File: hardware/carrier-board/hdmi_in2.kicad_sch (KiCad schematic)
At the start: 3 parts, among them J1 HDMI_TypeA_Receptacle, Q1 2N7002, U1 TXS0102DCUR

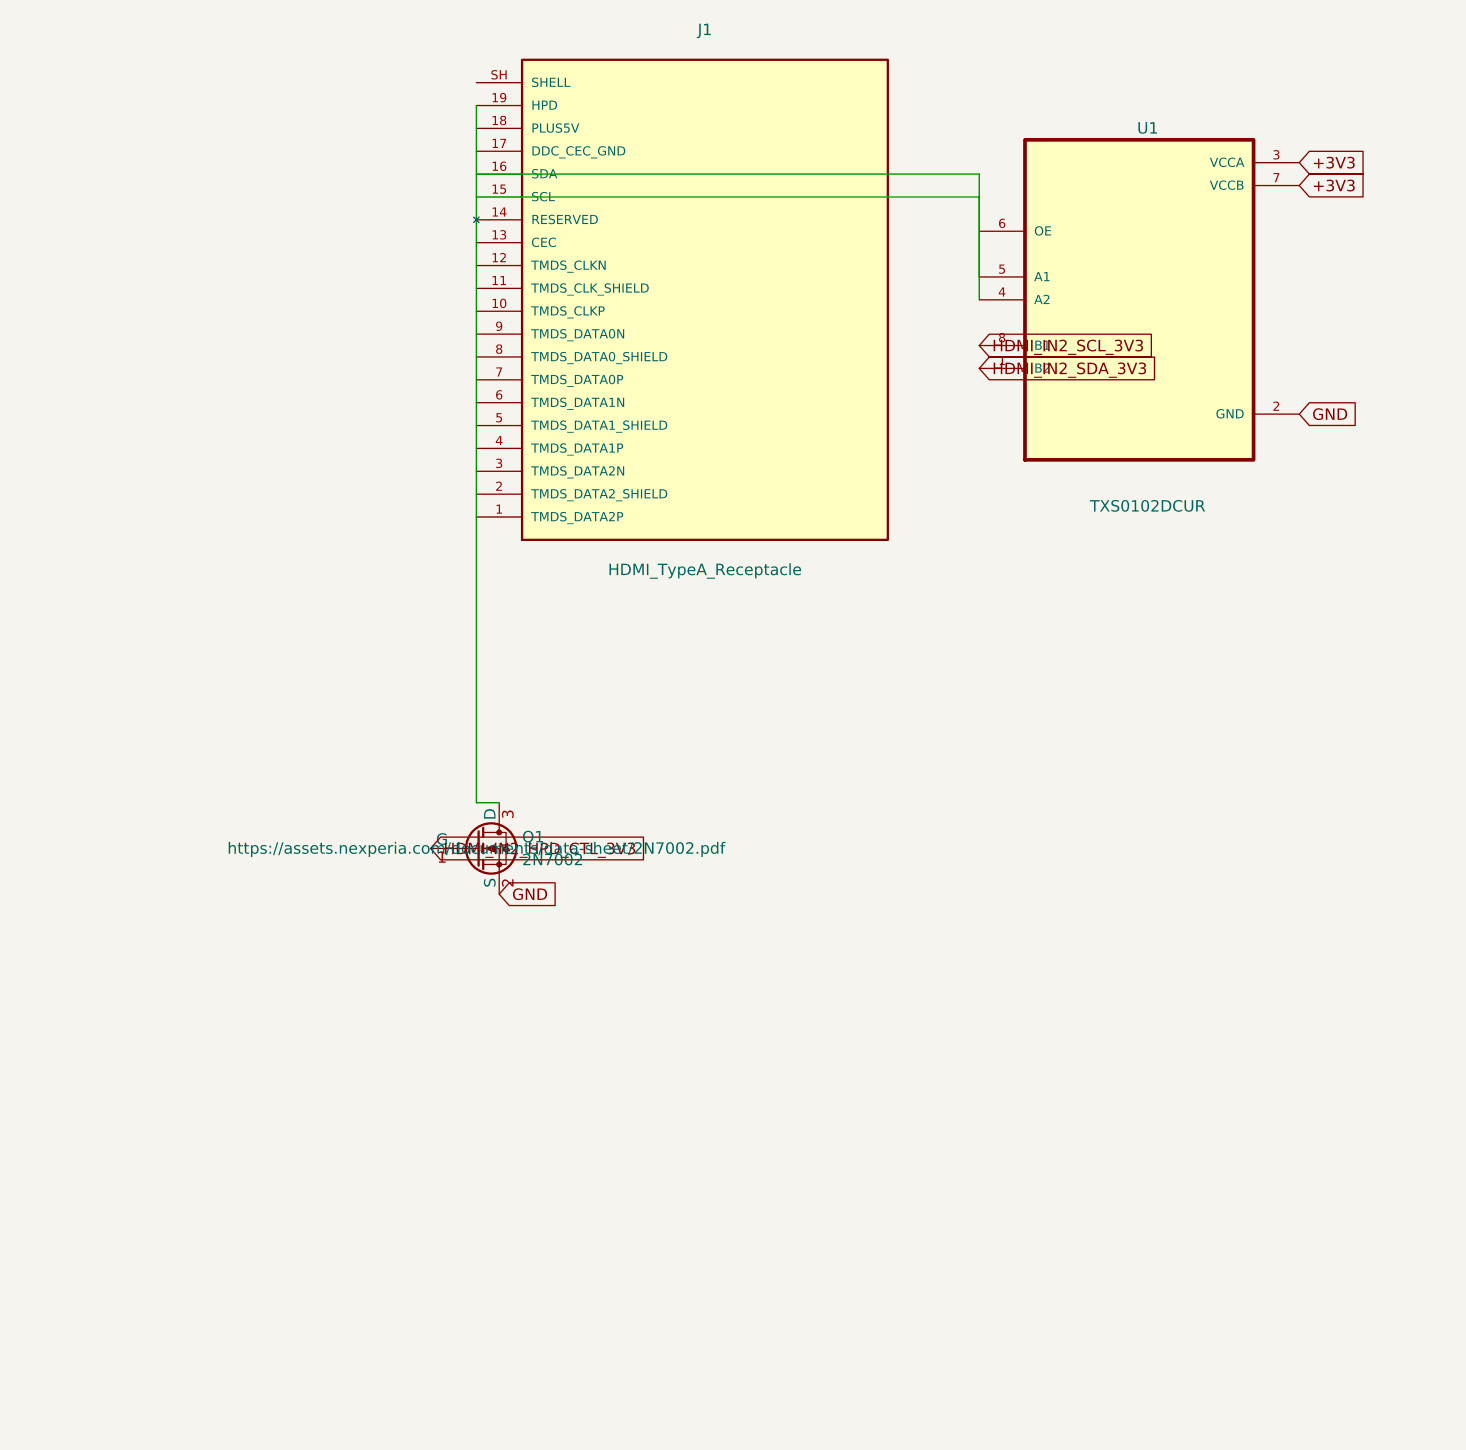
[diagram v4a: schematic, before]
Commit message: Wire TMDS data lines through TI TPD1E04U04 ESD protection
Switches ESD protection from the still-blocked Semtech RClamp0574P
(6+ failed attempts, including one wrong-part PDF caught via title
metadata) to TI TPD1E04U04: a real, fully-verified, HDMI 2.0-rated
single-channel ESD diode. Fetched TI's own datasheet directly and
hand-authored the symbol/footprint from its pin function table and
mechanical land-pattern drawing (1=IO, 2=GND, X1SON/DPY0002A).

Wires all 6 TMDS data lines (D0/D1/D2, P+N) per HDMI sheet from the
connector through a dedicated ESD diode to the exact SOM connector
B2B pin resolved from the TE0807 TRM in an earlier commit. Verified
by checking every one of the 48 affected pins (24 HDMI-side, 24
SOM-side) individually against the full-hierarchy ERC report, not
just that violation counts dropped.

TMDS_CLK is deliberately left unwired: doing this work surfaced a
real architecture question this project never actually settled --
whether each input port's GTH reference clock should come from the
Si5341A (already wired in the previous commit) or from the connector's
own TMDS_CLK pair, which has real wiring and part implications either
way. Documented in carrier-board-spec.md rather than guessed at.
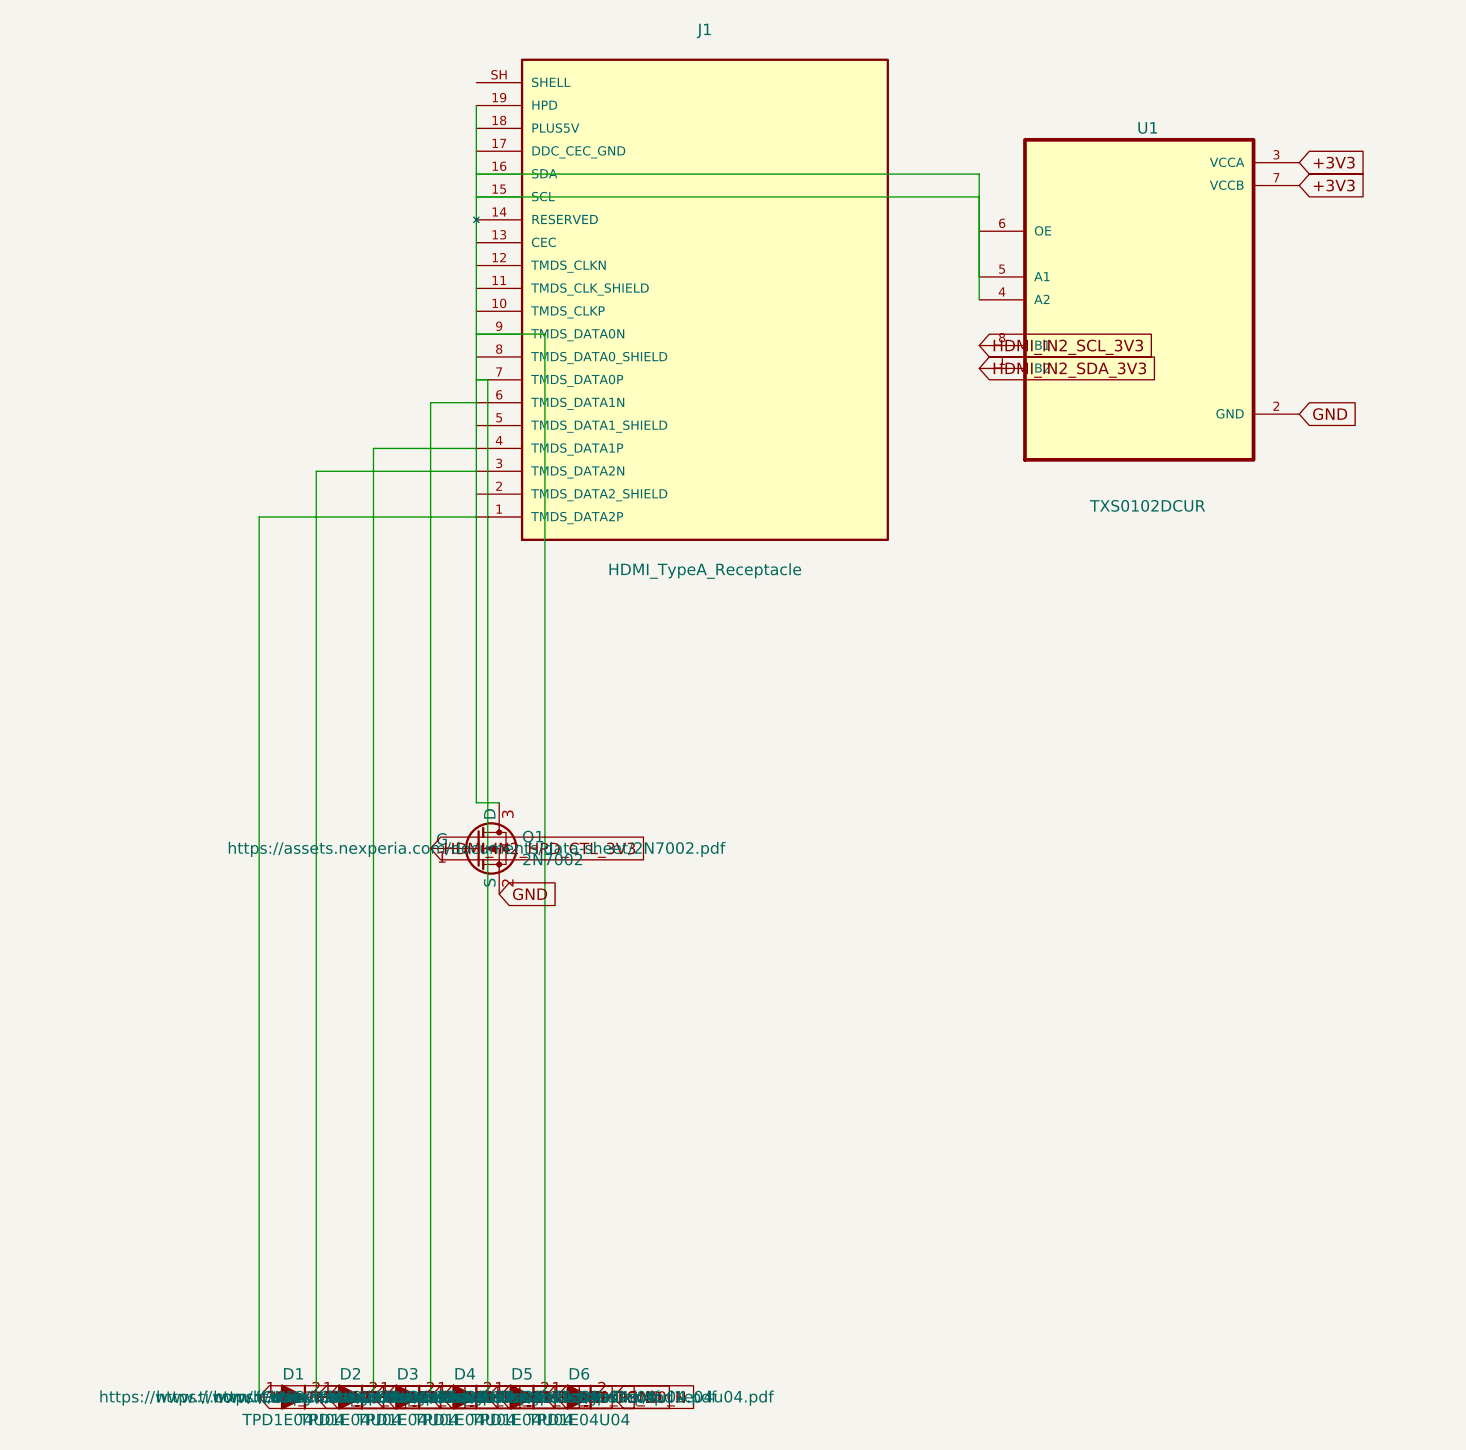
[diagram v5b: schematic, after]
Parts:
- added D1, D2, D3, D4, D5, D6: TPD1E04U04, carrier_footprints:X1SON-2_DPY0002A, symbol TPD1E04U04:TPD1E04U04
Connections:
- net GND: now also D1.2 (GND), D2.2 (GND), D3.2 (GND), D4.2 (GND), D5.2 (GND), D6.2 (GND)
- net HDMI_IN2_HPD_CTL_3V3: now also J1.6 (TMDS_DATA1N), D4.1 (IO)
- net IN2_TMDS_D2_P: now reaches J1.1 (TMDS_DATA2P)
- net IN2_TMDS_D2_P: now also D1.1 (IO)
- net IN2_TMDS_D2_N: now reaches J1.3 (TMDS_DATA2N)
- net IN2_TMDS_D2_N: now also D2.1 (IO)
- net IN2_TMDS_D1_P: now reaches J1.4 (TMDS_DATA1P)
- net IN2_TMDS_D1_P: now also D3.1 (IO)
- net IN2_TMDS_D0_P: now reaches J1.7 (TMDS_DATA0P)
- net IN2_TMDS_D0_P: now also D5.1 (IO)
- net IN2_TMDS_D0_N: now reaches J1.9 (TMDS_DATA0N)
- net IN2_TMDS_D0_N: now also D6.1 (IO)

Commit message: Resolve TMDS_CLK routing and wire it to the spare 4th GTH lane
Researched the open question from the previous commit (per user
direction): does each input port's GTH reference clock come from
Si5341A or from the connector's own TMDS_CLK pair? AMD's own GTH
documentation (PG380) confirms the RX CDR tracks incoming data up to
+/-1250ppm from the reference-derived rate below 6.6Gb/s -- comfortably
covering our ~5.94Gbps TMDS rate -- so a single reference only needs
coarse per-format tuning, which is exactly what the Si5341A (already
wired in an earlier commit) was chosen for. TMDS_CLK itself goes to
each quad's "spare" 4th GTH lane instead, using the identical
TPD1E04U04 ESD-diode wiring pattern already validated for TMDS_DATA0-2.

No rework of prior wiring was needed. Every one of the 16 affected
pins was checked individually against the ERC report.
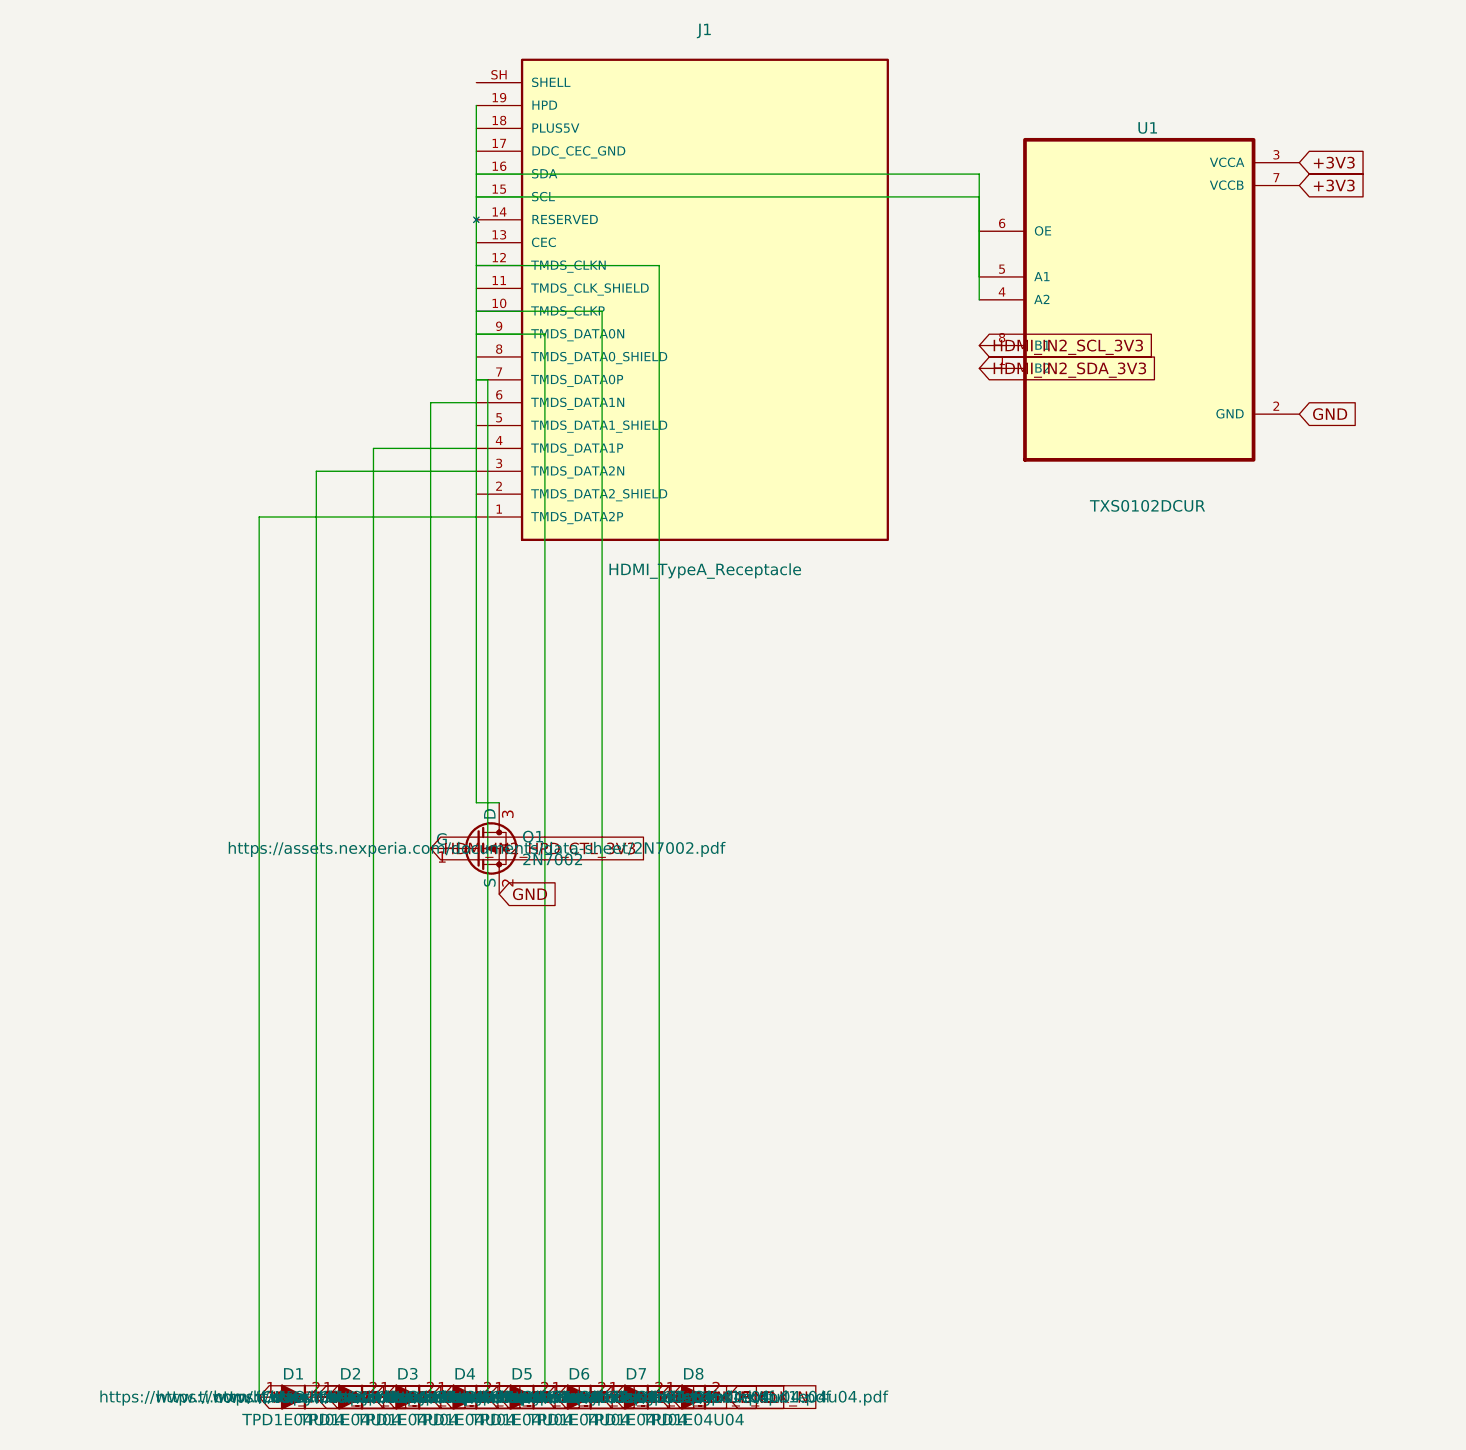
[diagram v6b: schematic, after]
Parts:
- added D7, D8: TPD1E04U04, carrier_footprints:X1SON-2_DPY0002A, symbol TPD1E04U04:TPD1E04U04
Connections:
- net GND: now also D7.2 (GND), D8.2 (GND)
- net IN2_TMDS_CLK_P: now reaches J1.10 (TMDS_CLKP)
- net IN2_TMDS_CLK_P: now also D7.1 (IO)
- net IN2_TMDS_CLK_N: now reaches J1.12 (TMDS_CLKN)
- net IN2_TMDS_CLK_N: now also D8.1 (IO)

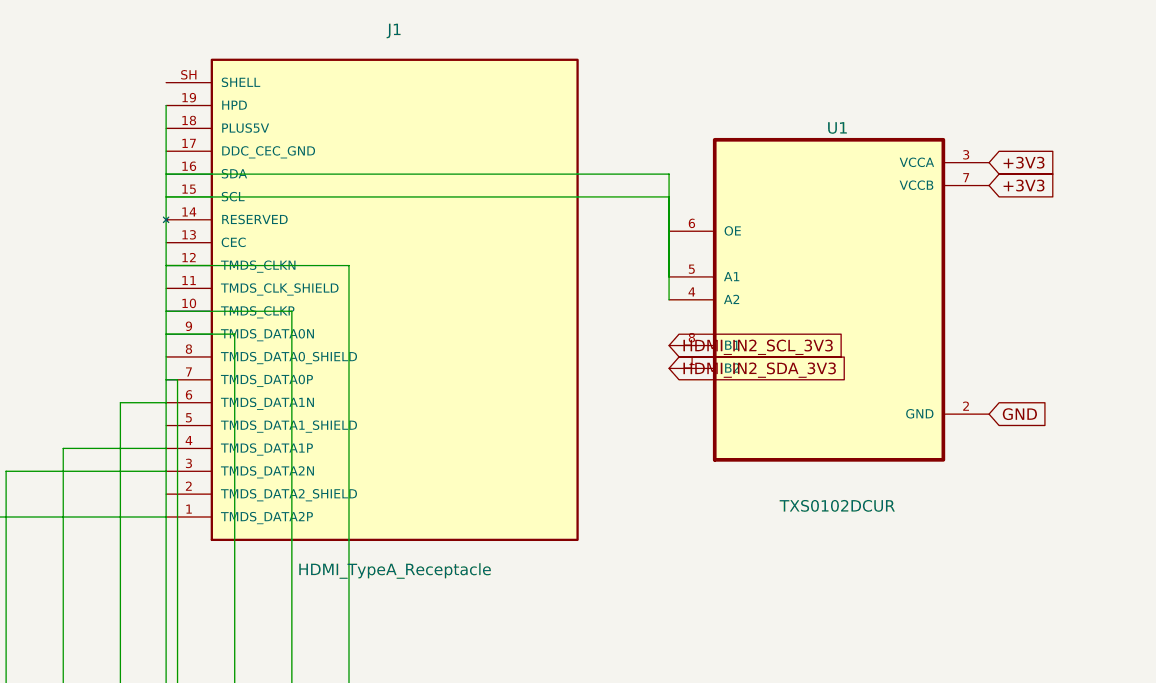
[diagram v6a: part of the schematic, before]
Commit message: Add decoupling capacitors to TXS0102 and Si5341A via Konnect MCP
Switches this project's KiCad schematic editing from hand-authored
S-expression scripts to Konnect's MCP tools, per the konnect skill's
operating rules -- a safer, validated API for schematic edits.

Ran Konnect's design_review/audit_decoupling for the first time on
this project and found a real, previously-missed gap: no decoupling
capacitors existed anywhere in the design. Adds 100nF caps for
TXS0102's VCCA/VCCB (all 4 HDMI sheets) and all 14 of Si5341A's
VDD-family pins (VDDA, VDD x3, VDDO0-9). These still show
power_pin_not_driven in ERC, correctly -- a capacitor doesn't power a
chip, and no regulator feeds these rails yet, which is the separate,
already-documented VCCO regulator open item.

Documents several real Konnect tool quirks discovered along the way:
connect_pins between exactly-coincident pins writes a zero-length
wire that doesn't register in net tracing; move_schematic_component
doesn't adjust connected wires; delete_schematic_net_label matches by
coordinate only and can delete an unrelated pre-existing label (this
happened to two legitimate Task-32 +3V3 labels, caught and restored);
batch_connect_to_net always creates local not global labels; and one
sequence of failed delete calls corrupted clocking.kicad_sch outright,
recovered via git checkout since nothing had been committed yet.
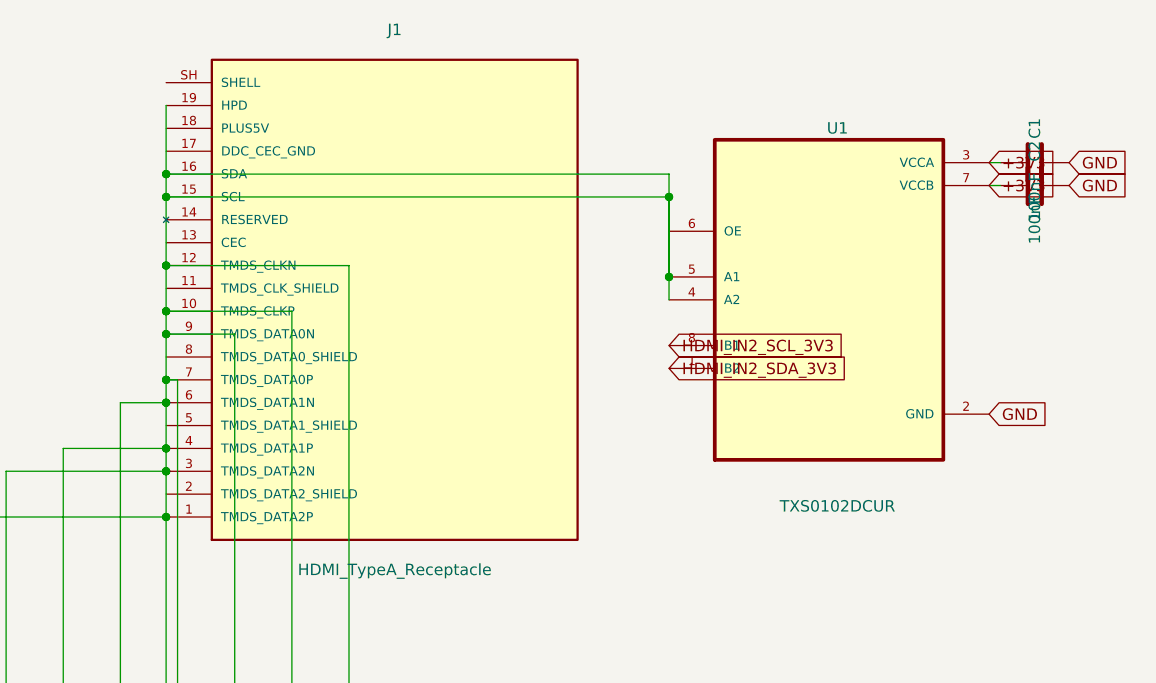
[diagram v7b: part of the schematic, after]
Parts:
- added C1, C2: 100nF, symbol Device:C
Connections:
- net IN2_TMDS_CLK_N is gone; now on net HDMI_IN2_HPD_CTL_3V3: D8.1 (IO), J1.12 (TMDS_CLKN)
- net IN2_TMDS_CLK_P is gone; now on net HDMI_IN2_HPD_CTL_3V3: D7.1 (IO), J1.10 (TMDS_CLKP)
- net IN2_TMDS_D0_N is gone; now on net HDMI_IN2_HPD_CTL_3V3: D6.1 (IO), J1.9 (TMDS_DATA0N)
- net IN2_TMDS_D0_P is gone; now on net HDMI_IN2_HPD_CTL_3V3: D5.1 (IO), J1.7 (TMDS_DATA0P)
- net IN2_TMDS_D1_P is gone; now on net HDMI_IN2_HPD_CTL_3V3: D3.1 (IO), J1.4 (TMDS_DATA1P)
- net IN2_TMDS_D2_N is gone; now on net HDMI_IN2_HPD_CTL_3V3: D2.1 (IO), J1.3 (TMDS_DATA2N)
- net IN2_TMDS_D2_P is gone; now on net HDMI_IN2_HPD_CTL_3V3: D1.1 (IO), J1.1 (TMDS_DATA2P)
- net +3V3: now also C1.1, C2.1
- net GND: now also C1.2, C2.2
- net HDMI_IN2_HPD_CTL_3V3: now also J1.15 (SCL), J1.16 (SDA), J1.19 (HPD), Q1.3 (D), U1.4 (A2), U1.5 (A1)

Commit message: Assign footprints to all new decoupling capacitors
Konnect's check_bom_health audit caught a real gap the ERC-based
workflow wouldn't have: add_schematic_component has no footprint
parameter, so all 22 new 100nF decoupling caps (C1/C2 in each HDMI
sheet, C3-C16 in clocking.kicad_sch) were missing one entirely --
would have blocked PCB layout. Assigned the standard
Capacitor_SMD:C_0402_1005Metric footprint to each.
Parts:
- C1, C2: footprint (none) -> Capacitor_SMD:C_0402_1005Metric
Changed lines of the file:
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@@
 			)
 		)
-		(property "Footprint" ""
+		(property "Footprint" "Capacitor_SMD:C_0402_1005Metric"
 			(at 121.92 83.82 0)
 			(hide yes)
@@
 			)
 		)
-		(property "Footprint" ""
+		(property "Footprint" "Capacitor_SMD:C_0402_1005Metric"
 			(at 121.92 86.36 0)
 			(hide yes)
